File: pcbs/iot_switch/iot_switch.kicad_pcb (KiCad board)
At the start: 2 copper layers, 18 parts, among them J1 AC IN, J2 LOAD OUT, K1 SANYOU_SRD_Form_C, Q1 BT136-500, Q2 BC547, SW1 L1 Switch, SW2 L2 Switch, U1 L7805, U2 ESP32-DEVKIT-V1, U3 MOC3021M

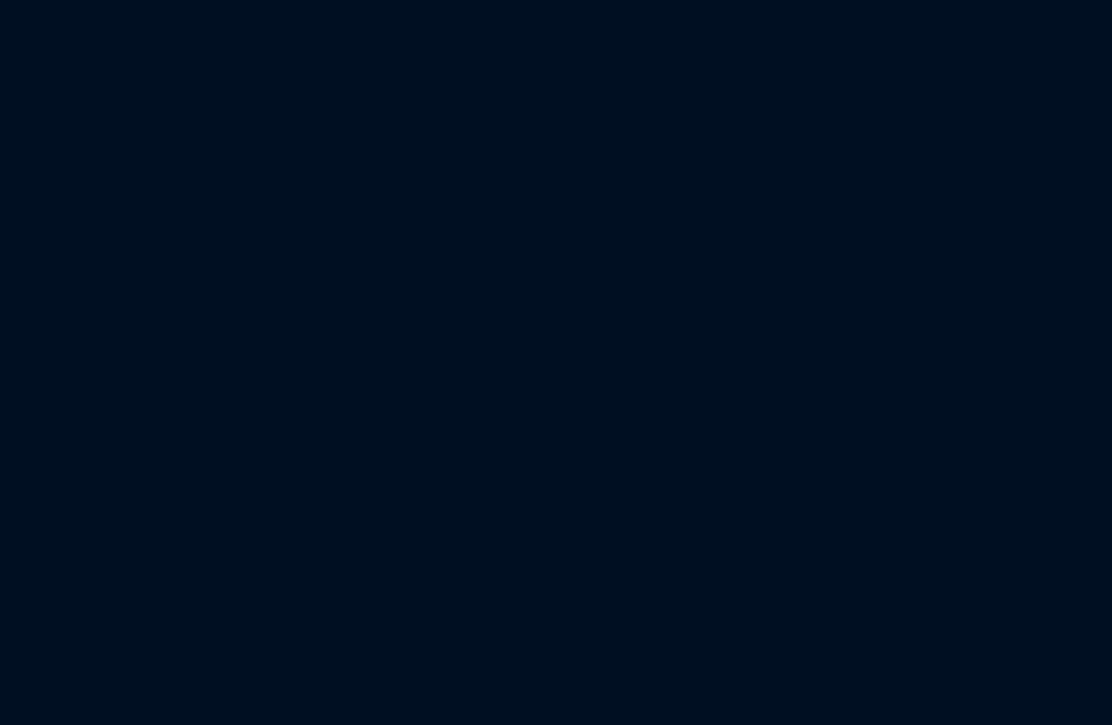
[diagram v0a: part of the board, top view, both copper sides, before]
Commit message: iot switch zv detection section added
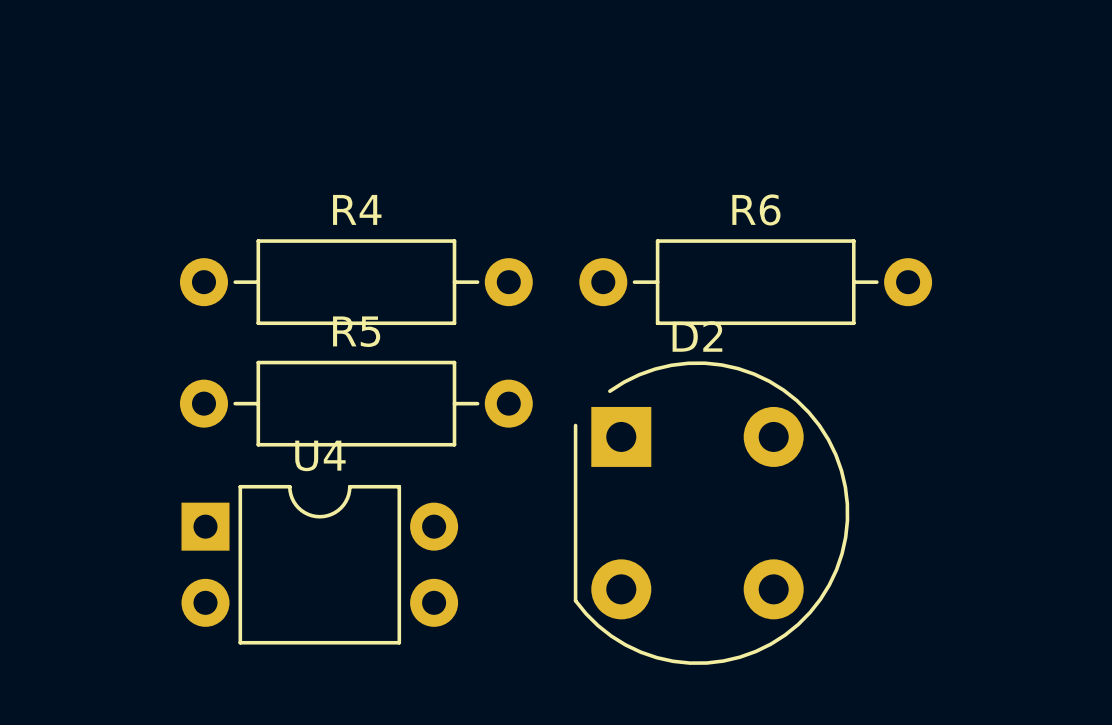
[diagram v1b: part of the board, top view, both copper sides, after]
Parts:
- added D2: W10G, Diode_THT:Diode_Bridge_Round_D9.8mm, F.Cu at (137.8, 138.8)
- added R4: 100k, Resistor_THT:R_Axial_DIN0207_L6.3mm_D2.5mm_P10.16mm_Horizontal, F.Cu at (123.9, 133.6)
- added R5: 100k, Resistor_THT:R_Axial_DIN0207_L6.3mm_D2.5mm_P10.16mm_Horizontal, F.Cu at (123.9, 137.7)
- added R6: 10k, Resistor_THT:R_Axial_DIN0207_L6.3mm_D2.5mm_P10.16mm_Horizontal, F.Cu at (137.2, 133.6)
- added U4: PC817, Package_DIP:DIP-4_W7.62mm, F.Cu at (123.9, 141.8)
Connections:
- U2 pad 9: Net-(U2-Pad9) -> ZVD
